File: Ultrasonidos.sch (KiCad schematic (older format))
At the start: 1 part, among them P12 CONN_01X04

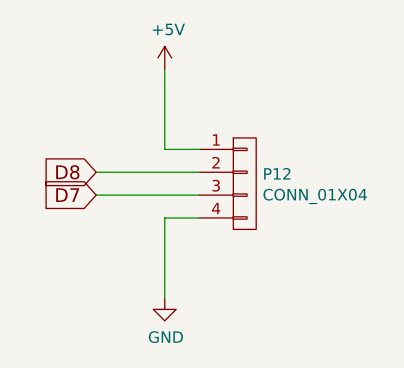
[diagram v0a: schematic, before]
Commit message: asignacion inicial de huellas
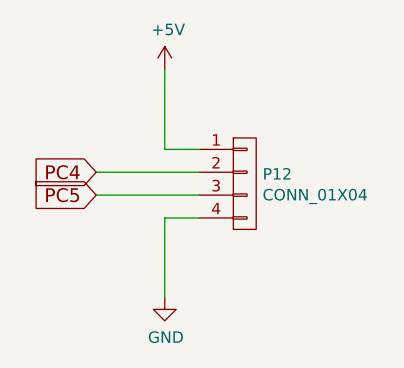
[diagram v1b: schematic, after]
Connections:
- net D7 renamed PC5
- net D8 renamed PC4
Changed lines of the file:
@@
 	3200 2450 3200 2800
 $Comp
-L GND #PWR85
+L GND #PWR0103
 U 1 1 588EAE81
 P 3200 2800
-F 0 "#PWR85" H 3200 2550 50  0001 C CNN
+F 0 "#PWR0103" H 3200 2550 50  0001 C CNN
 F 1 "GND" H 3205 2627 50  0000 C CNN
 F 2 "" H 3200 2800 50  0000 C CNN
@@
 	3200 2150 3200 1800
 $Comp
-L +5V #PWR84
+L +5V #PWR0104
 U 1 1 588EAE82
 P 3200 1800
-F 0 "#PWR84" H 3200 1650 50  0001 C CNN
+F 0 "#PWR0104" H 3200 1650 50  0001 C CNN
 F 1 "+5V" H 3215 1973 50  0000 C CNN
 F 2 "" H 3200 1800 50  0000 C CNN
@@
 	2900 2350 3350 2350
 Text GLabel 2900 2250 0    60   Input ~ 0
-D8
+PC4
 Text GLabel 2900 2350 0    60   Input ~ 0
-D7
+PC5
 $Bitmap
 Pos 5200 2350

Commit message: cambiar ch340T por ch340g y añadir nc a pines
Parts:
- P12: footprint Socket_Strips:Socket_Strip_Straight_1x04 -> Socket_Strips:Socket_Strip_Straight_1x04_Pitch2.54mm
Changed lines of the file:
@@
 $Descr User 8268 5846
 encoding utf-8
-Sheet 12 15
+Sheet 12 14
 Title "Puerto de expansión para sensor por ultrasonidos"
 Date "2017-01-25"
@@
 F 0 "P12" H 3628 2341 50  0000 L CNN
 F 1 "CONN_01X04" H 3628 2250 50  0000 L CNN
-F 2 "Socket_Strips:Socket_Strip_Straight_1x04" H 3550 2300 50  0001 C CNN
+F 2 "Socket_Strips:Socket_Strip_Straight_1x04_Pitch2.54mm" H 3550 2300 50  0001 C CNN
 F 3 "" H 3550 2300 50  0000 C CNN
 F 4 "NINIGI" H 3550 2300 60  0001 C CNN "Fabricante"
@@
 	3200 2450 3200 2800
 $Comp
-L GND #PWR0103
+L GND #PWR0111
 U 1 1 588EAE81
 P 3200 2800
-F 0 "#PWR0103" H 3200 2550 50  0001 C CNN
+F 0 "#PWR0111" H 3200 2550 50  0001 C CNN
 F 1 "GND" H 3205 2627 50  0000 C CNN
 F 2 "" H 3200 2800 50  0000 C CNN
@@
 	3200 2150 3200 1800
 $Comp
-L +5V #PWR0104
+L +5V #PWR0112
 U 1 1 588EAE82
 P 3200 1800
-F 0 "#PWR0104" H 3200 1650 50  0001 C CNN
+F 0 "#PWR0112" H 3200 1650 50  0001 C CNN
 F 1 "+5V" H 3215 1973 50  0000 C CNN
 F 2 "" H 3200 1800 50  0000 C CNN
